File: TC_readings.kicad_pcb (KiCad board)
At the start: 2 copper layers, 60.4 x 41.1 mm, 59 parts, among them J2 USB_B_Micro, J4 Conn_01x02_Pin

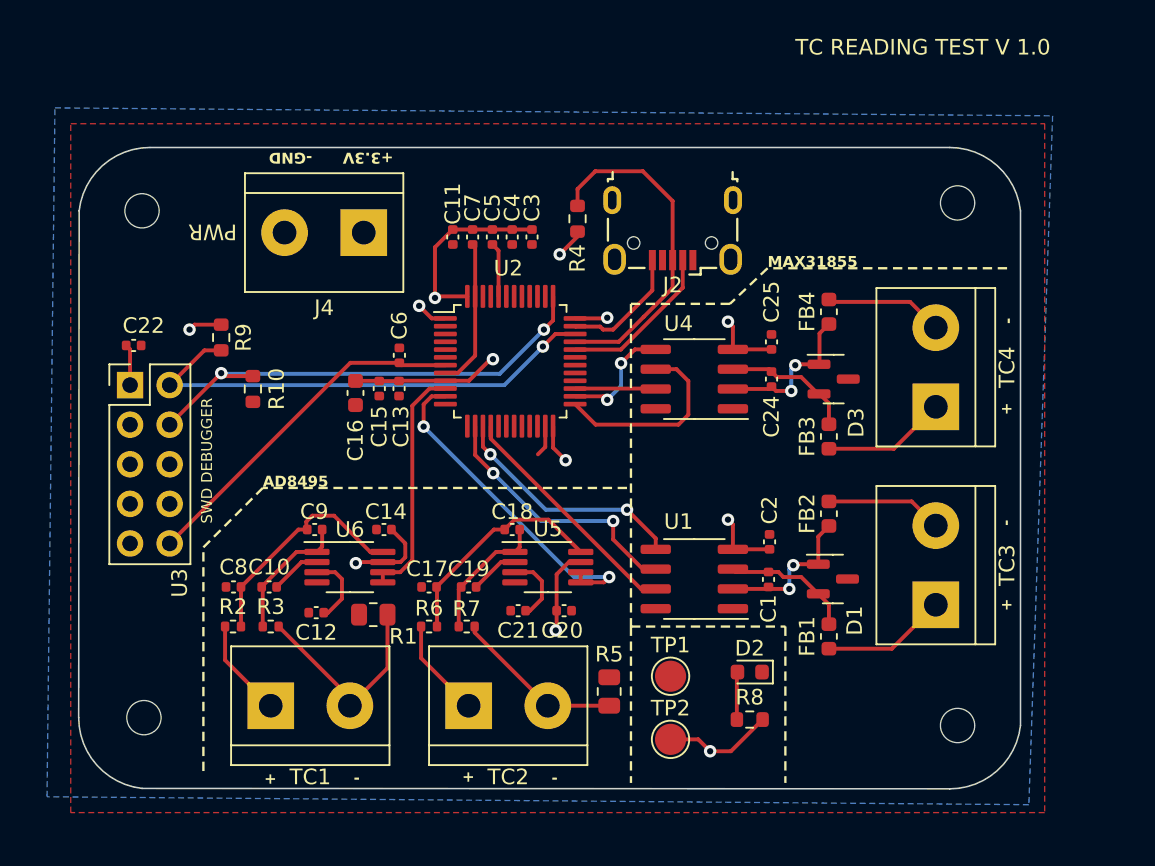
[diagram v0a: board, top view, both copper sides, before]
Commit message: Change to 4 layers
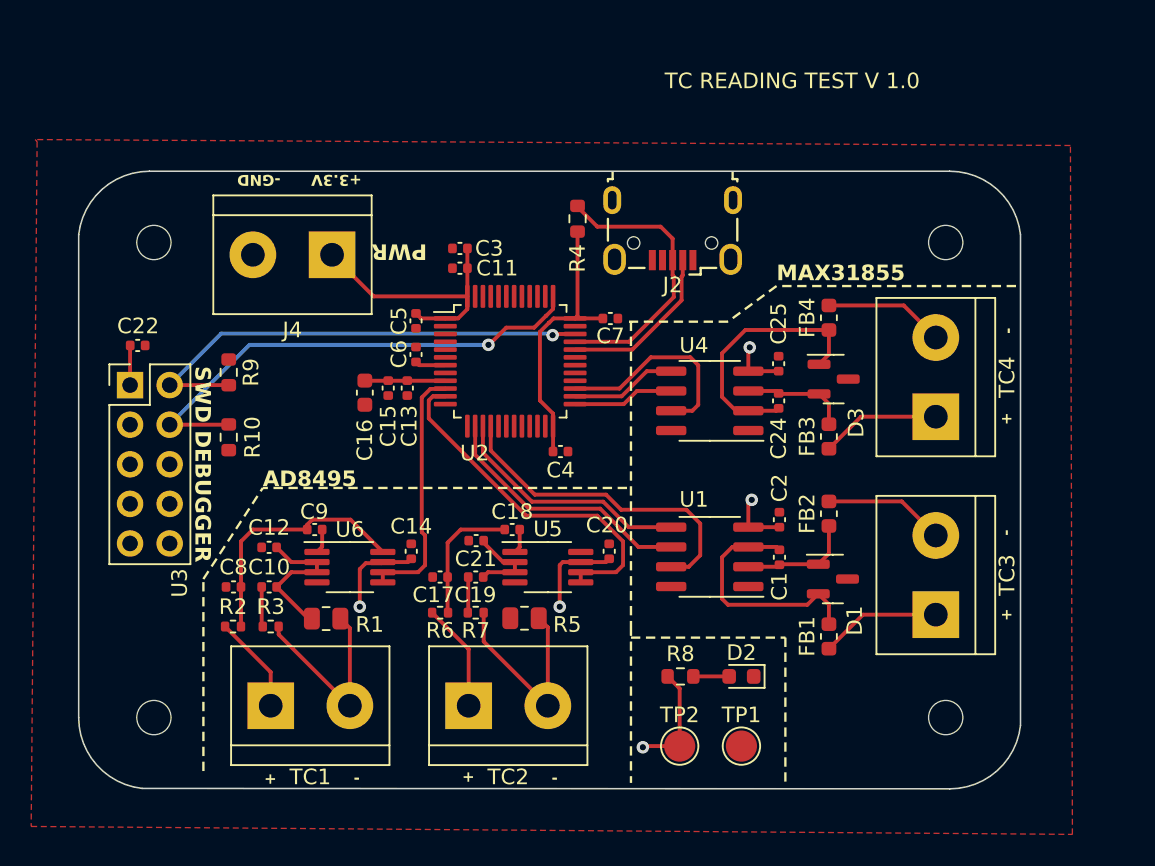
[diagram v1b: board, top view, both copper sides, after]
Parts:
- removed the REF** at (177.3, 117.3)
- removed the REF** at (125.0, 84.3)
- removed the REF** at (177.3, 83.8)
- removed the REF** at (125.1, 116.8)
- added G***: LOGO, me:petr, B.Cu at (137.7, 103.9)
- added REF**: MountingHole_2.2mm_M2, MountingHole:MountingHole_2.2mm_M2, F.Cu at (125.7, 116.8)
- added REF**: MountingHole_2.2mm_M2, MountingHole:MountingHole_2.2mm_M2, F.Cu at (176.5, 116.8)
- added REF**: MountingHole_2.2mm_M2, MountingHole:MountingHole_2.2mm_M2, F.Cu at (125.7, 86.4)
- added REF**: MountingHole_2.2mm_M2, MountingHole:MountingHole_2.2mm_M2, F.Cu at (176.5, 86.4)
- moved C4 14.1 mm to (151.8, 99.8), turned to 0 degrees
- moved C7 10.3 mm to (155.0, 91.2), turned to 0 degrees
- moved C5 7.28 mm to (142.5, 91.4)
- moved R5 7.18 mm to (149.5, 110.5), turned to 0 degrees
- moved TP1 6.38 mm to (163.4, 118.7)
- moved C21 5.24 mm to (146.4, 105.5), turned to 180 degrees
- moved R8 5.24 mm to (159.5, 114.2), turned to 180 degrees
- moved C12 5.17 mm to (133.1, 105.9), turned to 180 degrees
- moved C20 4.78 mm to (154.9, 106.2), turned to 90 degrees
- moved C3 4.68 mm to (145.4, 86.7), turned to 180 degrees
- moved R10 3.46 mm to (130.5, 98.9)
- moved R1 3.04 mm to (136.8, 110.5)
- moved J4 2.48 mm to (137.2, 87.1)
- moved R9 2.29 mm to (130.5, 94.7)
- moved C14 2.24 mm to (142.2, 106.2), turned to 90 degrees
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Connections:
- net Net-(J2-D+) renamed /D+
- net Net-(J2-D-) renamed /D-
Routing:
- net GND: track 38.6 -> 15.2 mm
- net nRST: track 22.5 -> 1.97 mm
- net TC_digital_2: track 5.19 -> 13.4 mm
- net +3.3V: track 61.6 -> 69.7 mm, vias 12 -> 5
- net Net-(U1-T+): track 8.36 -> 15.6 mm
- net Net-(U4-T-): track 10.1 -> 16.8 mm, vias 2 -> 0
- net nCS_2: track 12.6 -> 6.51 mm
- net Net-(U5-+IN): track 14.5 -> 8.52 mm
- net TC_digital_1: track 15.4 -> 21.2 mm
- net Net-(U5--IN): track 8.55 -> 3.86 mm
- net Net-(U6--IN): track 8.63 -> 4.15 mm
- net /D+: track 21.7 -> 18.3 mm
- net Net-(TC2--): track 11.0 -> 13.5 mm
- net Net-(U1-T-): track 9.72 -> 7.29 mm, vias 2 -> 0
- net TC_Out2: track 21.6 -> 23.1 mm, vias 2 -> 0
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- added copper zone on In2.Cu, net +3.3V
- added copper zone on In1.Cu, net GND
- removed copper zone on B.Cu, net +3.3V
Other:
- board size 60.4 x 41.1 mm -> 60.4 x 39.6 mm
- copper layers 2 -> 4

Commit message: TC Reading Test V1.0
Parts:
- removed the G*** at (137.7, 103.9)
- added G***: LOGO, me:UCIRP_logo, B.Cu at (163.8, 101.7)
- added G***: LOGO, me:petr_smaller_10mm, B.Cu at (132.7, 97.9)
- moved 3.3V 7.18 mm to (166.6, 118.1)
- moved GND 7.18 mm to (170.6, 118.1)
- moved 3.3V 5.98 mm to (158.9, 118.1), turned to 90 degrees
- moved R8 4.68 mm to (162.1, 118.1), turned to -90 degrees
- moved C21 1.19 mm to (146.4, 106.7), turned to 0 degrees
- moved C18 0.25 mm to (148.7, 104.5)
- moved C7 0.18 mm to (155.0, 91.1)
- moved C12 0.13 mm to (133.1, 106.0)
- renumbered TP2 to 3.3V, D2 to 3.3V, TP1 to GND
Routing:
- net GND: track 15.2 -> 37.1 mm, vias 0 -> 11
- net nRST: track 1.97 -> 22.6 mm
- net unconnected-(J2-Shield-Pad6): track 0.00 -> 15.5 mm
- net Net-(U6--IN): track 4.15 -> 12.3 mm
- net Net-(U5-+IN): track 8.52 -> 15.9 mm
- net Net-(U5--IN): track 3.86 -> 10.8 mm
- net Net-(TC1-+): track 7.56 -> 6.29 mm
- net TC_Out2: track 23.1 -> 24.2 mm
- net Net-(D2-A): track 2.30 -> 3.19 mm
- net +3.3V: track 69.7 -> 70.1 mm, vias 5 -> 8
- added copper zone on B.Cu, net GND
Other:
- board text added: "TC READING TEST V1.0"
- board text added: "TEST POINTS"
- board text added: "by: A. Zhang Jiang, G. Nguyen github.com/Ale-ZJ/TC_readings_testPCB commit hash:"
- board text removed: "TC READING TEST V 1.0"
